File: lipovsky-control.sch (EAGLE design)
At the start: 43 parts, among them J5 AVRISP0.1", P1 M04-929P, P2 M04-929P, P3 M04-929P, P4 M04-929P, U1 ATTINYX4A8MU, U2 MIC2288YD5, U3 MIC2288YD5, U7 LTV-816S

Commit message: .
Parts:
- renumbered U7 to U4
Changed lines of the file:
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@@
 <parts>
 <part name="R1" library="dubec" deviceset="POT" device="5K" value="POT5K"/>
-<part name="U7" library="dubec" deviceset="LTV-8" device="16S"/>
+<part name="U4" library="dubec" deviceset="LTV-8" device="16S"/>
 <part name="R3" library="dubec" deviceset="RES" device="330_16" value="RES330_16"/>
 <part name="U1" library="dubec" deviceset="ATTINYX4A" device="8MU"/>
@@
 <instances>
 <instance part="R1" gate="G$1" x="55.88" y="-43.18" rot="R180"/>
-<instance part="U7" gate="G$1" x="66.04" y="-25.4" rot="MR0"/>
+<instance part="U4" gate="G$1" x="66.04" y="-25.4" rot="MR0"/>
 <instance part="R3" gate="G$1" x="55.88" y="-33.02" rot="R90"/>
 <instance part="U1" gate="G$1" x="12.7" y="22.86"/>
@@
 <net name="FB" class="0">
 <segment>
-<pinref part="U7" gate="G$1" pin="E"/>
+<pinref part="U4" gate="G$1" pin="E"/>
 <wire x1="58.42" y1="-27.94" x2="55.88" y2="-27.94" width="0.1524" layer="91"/>
 <label x="53.34" y="-27.94" size="1.778" layer="95" rot="R90" xref="yes"/>
@@
 <net name="OPTO_A" class="0">
 <segment>
-<pinref part="U7" gate="G$1" pin="A"/>
+<pinref part="U4" gate="G$1" pin="A"/>
 <wire x1="73.66" y1="-22.86" x2="76.2" y2="-22.86" width="0.1524" layer="91"/>
 <label x="76.2" y="-22.86" size="1.778" layer="95" xref="yes"/>
@@
 <net name="OPTO_C" class="0">
 <segment>
-<pinref part="U7" gate="G$1" pin="K"/>
+<pinref part="U4" gate="G$1" pin="K"/>
 <wire x1="73.66" y1="-27.94" x2="76.2" y2="-27.94" width="0.1524" layer="91"/>
 <label x="76.2" y="-27.94" size="1.778" layer="95" xref="yes"/>
@@
 </segment>
 <segment>
-<pinref part="U7" gate="G$1" pin="C"/>
+<pinref part="U4" gate="G$1" pin="C"/>
 <wire x1="58.42" y1="-22.86" x2="55.88" y2="-22.86" width="0.1524" layer="91"/>
 <wire x1="55.88" y1="-22.86" x2="55.88" y2="-17.78" width="0.1524" layer="91"/>

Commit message: tidy
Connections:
- removed net !OE: J5.SCK, P3.3, U1.PA4
- removed net CP: J5.MISO, P3.2, U1.PA5
- removed net DS: J5.MOSI, P3.1, U1.PA6
- new net !S_RESET: P3.1
- new net MISO: J5.MISO, U1.PA5
- new net SCL: J5.SCK, P3.2, U1.PA4
- new net SDA: J5.MOSI, P3.3, U1.PA6
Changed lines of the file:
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@@
 </segment>
 </net>
-<net name="!OE" class="0">
-<segment>
-<label x="78.74" y="35.56" size="1.27" layer="95" rot="R90" xref="yes"/>
-<wire x1="78.74" y1="33.02" x2="78.74" y2="35.56" width="0.1524" layer="91"/>
-<pinref part="P3" gate="G$1" pin="3"/>
-</segment>
-<segment>
-<label x="-10.16" y="17.78" size="1.27" layer="95" rot="R180" xref="yes"/>
-<pinref part="U1" gate="G$1" pin="PA4"/>
-<wire x1="-10.16" y1="17.78" x2="2.54" y2="17.78" width="0.1524" layer="91"/>
-</segment>
-<segment>
-<pinref part="J5" gate="G$1" pin="SCK"/>
-<wire x1="119.38" y1="22.86" x2="121.92" y2="20.32" width="0.1524" layer="91"/>
-<label x="121.92" y="20.32" size="1.27" layer="95" xref="yes"/>
-</segment>
-</net>
-<net name="CP" class="0">
-<segment>
-<label x="81.28" y="35.56" size="1.27" layer="95" rot="R90" xref="yes"/>
-<wire x1="81.28" y1="33.02" x2="81.28" y2="35.56" width="0.1524" layer="91"/>
-<pinref part="P3" gate="G$1" pin="2"/>
-</segment>
+<net name="MISO" class="0">
 <segment>
 <label x="-10.16" y="15.24" size="1.27" layer="95" rot="R180" xref="yes"/>
@@
 <wire x1="119.38" y1="17.78" x2="121.92" y2="15.24" width="0.1524" layer="91"/>
 <label x="121.92" y="15.24" size="1.27" layer="95" xref="yes"/>
-</segment>
-</net>
-<net name="DS" class="0">
-<segment>
-<label x="83.82" y="35.56" size="1.27" layer="95" rot="R90" xref="yes"/>
-<wire x1="83.82" y1="33.02" x2="83.82" y2="35.56" width="0.1524" layer="91"/>
-<pinref part="P3" gate="G$1" pin="1"/>
-</segment>
-<segment>
-<label x="33.02" y="27.94" size="1.27" layer="95" xref="yes"/>
-<pinref part="U1" gate="G$1" pin="PA6"/>
-<wire x1="33.02" y1="27.94" x2="22.86" y2="27.94" width="0.1524" layer="91"/>
-</segment>
-<segment>
-<pinref part="J5" gate="G$1" pin="MOSI"/>
-<wire x1="104.14" y1="22.86" x2="101.6" y2="20.32" width="0.1524" layer="91"/>
-<label x="101.6" y="20.32" size="1.27" layer="95" rot="R180" xref="yes"/>
 </segment>
 </net>
@@
 </segment>
 </net>
+<net name="SDA" class="0">
+<segment>
+<pinref part="P3" gate="G$1" pin="3"/>
+<wire x1="78.74" y1="33.02" x2="78.74" y2="35.56" width="0.1524" layer="91"/>
+<label x="78.74" y="35.56" size="1.27" layer="95" rot="R90" xref="yes"/>
+</segment>
+<segment>
+<label x="33.02" y="27.94" size="1.27" layer="95" xref="yes"/>
+<pinref part="U1" gate="G$1" pin="PA6"/>
+<wire x1="33.02" y1="27.94" x2="22.86" y2="27.94" width="0.1524" layer="91"/>
+</segment>
+<segment>
+<pinref part="J5" gate="G$1" pin="MOSI"/>
+<wire x1="104.14" y1="22.86" x2="101.6" y2="20.32" width="0.1524" layer="91"/>
+<label x="101.6" y="20.32" size="1.27" layer="95" rot="R180" xref="yes"/>
+</segment>
+</net>
+<net name="SCL" class="0">
+<segment>
+<pinref part="P3" gate="G$1" pin="2"/>
+<wire x1="81.28" y1="33.02" x2="81.28" y2="35.56" width="0.1524" layer="91"/>
+<label x="81.28" y="35.56" size="1.27" layer="95" rot="R90" xref="yes"/>
+</segment>
+<segment>
+<label x="-10.16" y="17.78" size="1.27" layer="95" rot="R180" xref="yes"/>
+<pinref part="U1" gate="G$1" pin="PA4"/>
+<wire x1="-10.16" y1="17.78" x2="2.54" y2="17.78" width="0.1524" layer="91"/>
+</segment>
+<segment>
+<pinref part="J5" gate="G$1" pin="SCK"/>
+<wire x1="119.38" y1="22.86" x2="121.92" y2="20.32" width="0.1524" layer="91"/>
+<label x="121.92" y="20.32" size="1.27" layer="95" xref="yes"/>
+</segment>
+</net>
+<net name="!S_RESET" class="0">
+<segment>
+<pinref part="P3" gate="G$1" pin="1"/>
+<wire x1="83.82" y1="33.02" x2="83.82" y2="35.56" width="0.1524" layer="91"/>
+<label x="83.82" y="35.56" size="1.27" layer="95" rot="R90" xref="yes"/>
+</segment>
+</net>

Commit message: neverending gilding
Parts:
- added R16, R17: RES4.7K_16, dubec:RES4.7K_16
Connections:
- net !RESET: now also R15.1; no longer R15.2
- net +5V: now also R15.2, R16.2, R17.1; no longer R15.1
- net SCL: now also R17.2
- net SDA: now also R16.1
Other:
- moved on the sheet: R10, R15, R7, R8, R9
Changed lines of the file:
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@@
 <part name="J5" library="dubec" deviceset="AVRISP" device="0.1&quot;" value="AVRISP0.1&quot;"/>
 <part name="R15" library="dubec" deviceset="RES" device="10K_16"/>
+<part name="R16" library="dubec" deviceset="RES" device="4.7K_16" value="RES4.7K_16"/>
+<part name="R17" library="dubec" deviceset="RES" device="4.7K_16" value="RES4.7K_16"/>
 </parts>
 <sheets>
@@
 <instance part="D4" gate="G$1" x="-2.54" y="-22.86"/>
 <instance part="D5" gate="G$1" x="-2.54" y="-38.1"/>
-<instance part="R7" gate="G$1" x="27.94" y="25.4"/>
-<instance part="R8" gate="G$1" x="27.94" y="17.78"/>
-<instance part="R9" gate="G$1" x="27.94" y="20.32"/>
-<instance part="R10" gate="G$1" x="27.94" y="22.86"/>
+<instance part="R7" gate="G$1" x="30.48" y="25.4"/>
+<instance part="R8" gate="G$1" x="30.48" y="17.78"/>
+<instance part="R9" gate="G$1" x="30.48" y="20.32"/>
+<instance part="R10" gate="G$1" x="30.48" y="22.86"/>
 <instance part="R11" gate="G$1" x="5.08" y="-40.64" rot="R90"/>
 <instance part="R12" gate="G$1" x="10.16" y="-35.56" rot="R180"/>
@@
 <instance part="C3" gate="G$1" x="43.18" y="-35.56" rot="R90"/>
 <instance part="J5" gate="G$1" x="111.76" y="22.86"/>
-<instance part="R15" gate="G$1" x="25.4" y="10.16" rot="R90"/>
+<instance part="R15" gate="G$1" x="30.48" y="15.24"/>
+<instance part="R16" gate="G$1" x="30.48" y="27.94"/>
+<instance part="R17" gate="G$1" x="-5.08" y="17.78"/>
 </instances>
 <busses>
@@
 <segment>
 <pinref part="U1" gate="G$1" pin="PB3"/>
-<wire x1="22.86" y1="15.24" x2="25.4" y2="15.24" width="0.1524" layer="91"/>
-<label x="33.02" y="15.24" size="1.27" layer="95" xref="yes"/>
-<pinref part="R15" gate="G$1" pin="2"/>
-<wire x1="25.4" y1="15.24" x2="33.02" y2="15.24" width="0.1524" layer="91"/>
-<wire x1="25.4" y1="15.24" x2="25.4" y2="12.7" width="0.1524" layer="91"/>
-<junction x="25.4" y="15.24"/>
+<label x="25.4" y="15.24" size="1.27" layer="95" rot="R270" xref="yes"/>
+<pinref part="R15" gate="G$1" pin="1"/>
+<wire x1="22.86" y1="15.24" x2="27.94" y2="15.24" width="0.1524" layer="91"/>
 </segment>
 <segment>
@@
 </segment>
 <segment>
-<pinref part="R15" gate="G$1" pin="1"/>
-<wire x1="25.4" y1="7.62" x2="25.4" y2="5.08" width="0.1524" layer="91"/>
-<label x="25.4" y="5.08" size="1.27" layer="95" rot="R270" xref="yes"/>
-</segment>
-<segment>
 <pinref part="J5" gate="G$1" pin="VCC"/>
 <wire x1="104.14" y1="17.78" x2="101.6" y2="15.24" width="0.1524" layer="91"/>
 <label x="101.6" y="15.24" size="1.27" layer="95" rot="R180" xref="yes"/>
+</segment>
+<segment>
+<pinref part="R17" gate="G$1" pin="1"/>
+<wire x1="-7.62" y1="17.78" x2="-10.16" y2="17.78" width="0.1524" layer="91"/>
+<label x="-10.16" y="17.78" size="1.27" layer="95" rot="R180" xref="yes"/>
+</segment>
+<segment>
+<pinref part="R16" gate="G$1" pin="2"/>
+<wire x1="33.02" y1="27.94" x2="35.56" y2="27.94" width="0.1524" layer="91"/>
+<label x="35.56" y="27.94" size="1.27" layer="95" xref="yes"/>
+</segment>
+<segment>
+<pinref part="R15" gate="G$1" pin="2"/>
+<wire x1="33.02" y1="15.24" x2="35.56" y2="15.24" width="0.1524" layer="91"/>
+<label x="35.56" y="15.24" size="1.27" layer="95" xref="yes"/>
 </segment>
 </net>
@@
 </segment>
 <segment>
-<label x="33.02" y="25.4" size="1.27" layer="95" xref="yes"/>
+<label x="35.56" y="25.4" size="1.27" layer="95" xref="yes"/>
 <pinref part="R7" gate="G$1" pin="2"/>
-<wire x1="30.48" y1="25.4" x2="33.02" y2="25.4" width="0.1524" layer="91"/>
+<wire x1="33.02" y1="25.4" x2="35.56" y2="25.4" width="0.1524" layer="91"/>
 </segment>
 </net>
@@
 </segment>
 <segment>
-<label x="33.02" y="17.78" size="1.27" layer="95" xref="yes"/>
+<label x="35.56" y="17.78" size="1.27" layer="95" xref="yes"/>
 <pinref part="R8" gate="G$1" pin="2"/>
-<wire x1="30.48" y1="17.78" x2="33.02" y2="17.78" width="0.1524" layer="91"/>
+<wire x1="33.02" y1="17.78" x2="35.56" y2="17.78" width="0.1524" layer="91"/>
 </segment>
 </net>
@@
 </segment>
 <segment>
-<label x="33.02" y="20.32" size="1.27" layer="95" xref="yes"/>
+<label x="35.56" y="20.32" size="1.27" layer="95" xref="yes"/>
 <pinref part="R9" gate="G$1" pin="2"/>
-<wire x1="33.02" y1="20.32" x2="30.48" y2="20.32" width="0.1524" layer="91"/>
+<wire x1="35.56" y1="20.32" x2="33.02" y2="20.32" width="0.1524" layer="91"/>
 </segment>
 </net>
@@
 </segment>
 <segment>
-<label x="33.02" y="22.86" size="1.27" layer="95" xref="yes"/>
+<label x="35.56" y="22.86" size="1.27" layer="95" xref="yes"/>
 <pinref part="R10" gate="G$1" pin="2"/>
-<wire x1="33.02" y1="22.86" x2="30.48" y2="22.86" width="0.1524" layer="91"/>
+<wire x1="35.56" y1="22.86" x2="33.02" y2="22.86" width="0.1524" layer="91"/>
 </segment>
 </net>
@@
 <pinref part="U1" gate="G$1" pin="PB0"/>
 <pinref part="R10" gate="G$1" pin="1"/>
-<wire x1="22.86" y1="22.86" x2="25.4" y2="22.86" width="0.1524" layer="91"/>
+<wire x1="22.86" y1="22.86" x2="27.94" y2="22.86" width="0.1524" layer="91"/>
 </segment>
 </net>
@@
 <pinref part="U1" gate="G$1" pin="PB1"/>
 <pinref part="R9" gate="G$1" pin="1"/>
-<wire x1="22.86" y1="20.32" x2="25.4" y2="20.32" width="0.1524" layer="91"/>
+<wire x1="22.86" y1="20.32" x2="27.94" y2="20.32" width="0.1524" layer="91"/>
 </segment>
 </net>
@@
 <pinref part="U1" gate="G$1" pin="PB2"/>
 <pinref part="R8" gate="G$1" pin="1"/>
-<wire x1="22.86" y1="17.78" x2="25.4" y2="17.78" width="0.1524" layer="91"/>
+<wire x1="22.86" y1="17.78" x2="27.94" y2="17.78" width="0.1524" layer="91"/>
 </segment>
 </net>
@@
 <pinref part="U1" gate="G$1" pin="PA7"/>
 <pinref part="R7" gate="G$1" pin="1"/>
-<wire x1="22.86" y1="25.4" x2="25.4" y2="25.4" width="0.1524" layer="91"/>
+<wire x1="22.86" y1="25.4" x2="27.94" y2="25.4" width="0.1524" layer="91"/>
 </segment>
 </net>
@@
 </segment>
 <segment>
-<label x="33.02" y="27.94" size="1.27" layer="95" xref="yes"/>
+<label x="25.4" y="27.94" size="1.27" layer="95" rot="R90" xref="yes"/>
 <pinref part="U1" gate="G$1" pin="PA6"/>
-<wire x1="33.02" y1="27.94" x2="22.86" y2="27.94" width="0.1524" layer="91"/>
+<pinref part="R16" gate="G$1" pin="1"/>
+<wire x1="22.86" y1="27.94" x2="27.94" y2="27.94" width="0.1524" layer="91"/>
 </segment>
 <segment>
@@
 </segment>
 <segment>
-<label x="-10.16" y="17.78" size="1.27" layer="95" rot="R180" xref="yes"/>
+<label x="0" y="17.78" size="1.27" layer="95" rot="R90" xref="yes"/>
 <pinref part="U1" gate="G$1" pin="PA4"/>
-<wire x1="-10.16" y1="17.78" x2="2.54" y2="17.78" width="0.1524" layer="91"/>
-</segment>
-<segment>
+<pinref part="R17" gate="G$1" pin="2"/>
+<wire x1="2.54" y1="17.78" x2="-2.54" y2="17.78" width="0.1524" layer="91"/>
+</segment>
+<segment>

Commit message: tweaks
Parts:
- added U$2: JUMPER-PAD, dubec:JUMPER-PAD
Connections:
- net !S_RESET: now also U$2.1
- net MISO: now also U$2.2
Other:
- moved on the sheet: C1, C2, J5, P1, P2, P3, P4, R10, R13, R15, R16, R17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

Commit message: Connector pin reordering
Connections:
- net +5V: now also P4.4; no longer P4.2
- net +8V: now also P4.2; no longer P4.1
- net OPTO_C: now also P2.4; no longer P2.2
- net S+: now also P4.1; no longer P4.3
- net S-: now also P2.2, P3.3, P4.3; no longer P2.4, P3.4, P4.4
- net SCL: now also P3.4; no longer P3.2
- net SDA: now also P3.2; no longer P3.3
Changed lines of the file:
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@@
 </segment>
 <segment>
-<label x="93.98" y="12.7" size="1.27" layer="95" rot="R270" xref="yes"/>
-<wire x1="93.98" y1="15.24" x2="93.98" y2="12.7" width="0.1524" layer="91"/>
-<pinref part="P2" gate="G$1" pin="4"/>
-</segment>
-<segment>
-<label x="86.36" y="35.56" size="1.27" layer="95" rot="R90" xref="yes"/>
-<wire x1="86.36" y1="33.02" x2="86.36" y2="35.56" width="0.1524" layer="91"/>
-<pinref part="P3" gate="G$1" pin="4"/>
-</segment>
-<segment>
-<label x="66.04" y="35.56" size="1.27" layer="95" rot="R90" xref="yes"/>
-<wire x1="66.04" y1="33.02" x2="66.04" y2="35.56" width="0.1524" layer="91"/>
-<pinref part="P4" gate="G$1" pin="4"/>
+<label x="88.9" y="12.7" size="1.27" layer="95" rot="R270" xref="yes"/>
+<pinref part="P2" gate="G$1" pin="2"/>
+<wire x1="88.9" y1="12.7" x2="88.9" y2="15.24" width="0.1524" layer="91"/>
+</segment>
+<segment>
+<label x="88.9" y="35.56" size="1.27" layer="95" rot="R90" xref="yes"/>
+<pinref part="P3" gate="G$1" pin="3"/>
+<wire x1="88.9" y1="35.56" x2="88.9" y2="33.02" width="0.1524" layer="91"/>
+</segment>
+<segment>
+<label x="68.58" y="35.56" size="1.27" layer="95" rot="R90" xref="yes"/>
+<pinref part="P4" gate="G$1" pin="3"/>
+<wire x1="68.58" y1="35.56" x2="68.58" y2="33.02" width="0.1524" layer="91"/>
 </segment>
 <segment>
@@
 <segment>
 <label x="91.44" y="12.7" size="1.27" layer="95" rot="R270" xref="yes"/>
-<wire x1="91.44" y1="15.24" x2="91.44" y2="12.7" width="0.1524" layer="91"/>
 <pinref part="P2" gate="G$1" pin="3"/>
+<wire x1="91.44" y1="12.7" x2="91.44" y2="15.24" width="0.1524" layer="91"/>
 </segment>
 </net>
@@
 </segment>
 <segment>
-<label x="88.9" y="12.7" size="1.27" layer="95" rot="R270" xref="yes"/>
-<wire x1="88.9" y1="15.24" x2="88.9" y2="12.7" width="0.1524" layer="91"/>
-<pinref part="P2" gate="G$1" pin="2"/>
+<label x="93.98" y="12.7" size="1.27" layer="95" rot="R270" xref="yes"/>
+<pinref part="P2" gate="G$1" pin="4"/>
+<wire x1="93.98" y1="12.7" x2="93.98" y2="15.24" width="0.1524" layer="91"/>
 </segment>
 </net>
@@
 </segment>
 <segment>
-<label x="71.12" y="35.56" size="1.27" layer="95" rot="R90" xref="yes"/>
-<pinref part="P4" gate="G$1" pin="2"/>
-<wire x1="71.12" y1="35.56" x2="71.12" y2="33.02" width="0.1524" layer="91"/>
+<label x="66.04" y="35.56" size="1.27" layer="95" rot="R90" xref="yes"/>
+<pinref part="P4" gate="G$1" pin="4"/>
+<wire x1="66.04" y1="35.56" x2="66.04" y2="33.02" width="0.1524" layer="91"/>
 </segment>
 <segment>
@@
 <net name="S+" class="0">
 <segment>
-<label x="68.58" y="35.56" size="1.27" layer="95" rot="R90" xref="yes"/>
-<pinref part="P4" gate="G$1" pin="3"/>
-<wire x1="68.58" y1="35.56" x2="68.58" y2="33.02" width="0.1524" layer="91"/>
+<label x="73.66" y="35.56" size="1.27" layer="95" rot="R90" xref="yes"/>
+<pinref part="P4" gate="G$1" pin="1"/>
+<wire x1="73.66" y1="35.56" x2="73.66" y2="33.02" width="0.1524" layer="91"/>
 </segment>
 <segment>
@@
 <net name="+8V" class="0">
 <segment>
-<label x="73.66" y="35.56" size="1.27" layer="95" rot="R90" xref="yes"/>
-<wire x1="73.66" y1="33.02" x2="73.66" y2="35.56" width="0.1524" layer="91"/>
-<pinref part="P4" gate="G$1" pin="1"/>
+<label x="71.12" y="35.56" size="1.27" layer="95" rot="R90" xref="yes"/>
+<pinref part="P4" gate="G$1" pin="2"/>
+<wire x1="71.12" y1="35.56" x2="71.12" y2="33.02" width="0.1524" layer="91"/>
 </segment>
 <segment>
@@
 <net name="SDA" class="0">
 <segment>
-<pinref part="P3" gate="G$1" pin="3"/>
-<wire x1="88.9" y1="33.02" x2="88.9" y2="35.56" width="0.1524" layer="91"/>
-<label x="88.9" y="35.56" size="1.27" layer="95" rot="R90" xref="yes"/>
+<label x="91.44" y="35.56" size="1.27" layer="95" rot="R90" xref="yes"/>
+<pinref part="P3" gate="G$1" pin="2"/>
+<wire x1="91.44" y1="35.56" x2="91.44" y2="33.02" width="0.1524" layer="91"/>
 </segment>
 <segment>
@@
 <net name="SCL" class="0">
 <segment>
-<pinref part="P3" gate="G$1" pin="2"/>
-<wire x1="91.44" y1="33.02" x2="91.44" y2="35.56" width="0.1524" layer="91"/>
-<label x="91.44" y="35.56" size="1.27" layer="95" rot="R90" xref="yes"/>
-</segment>
-<segment>
+<label x="86.36" y="35.56" size="1.27" layer="95" rot="R90" xref="yes"/>
+<pinref part="P3" gate="G$1" pin="4"/>
+<wire x1="86.36" y1="35.56" x2="86.36" y2="33.02" width="0.1524" layer="91"/>
+</segment>
+<segment>

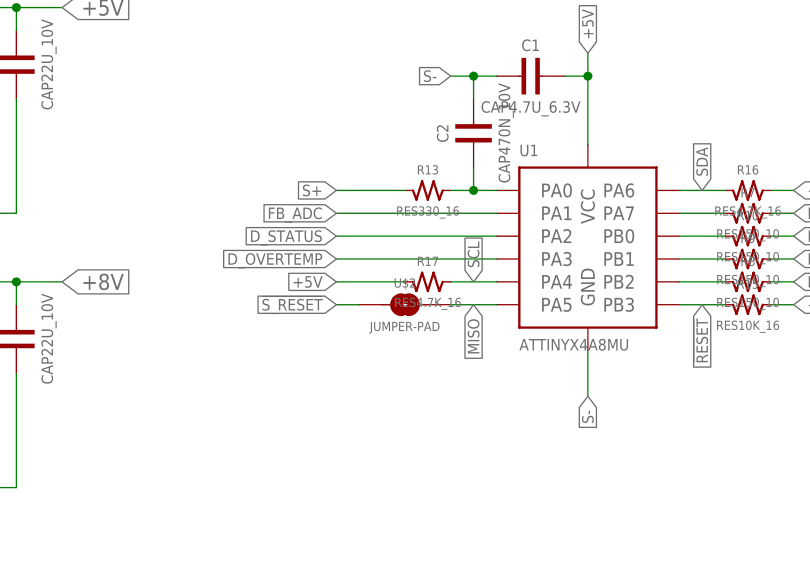
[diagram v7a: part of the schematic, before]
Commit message: Label fix
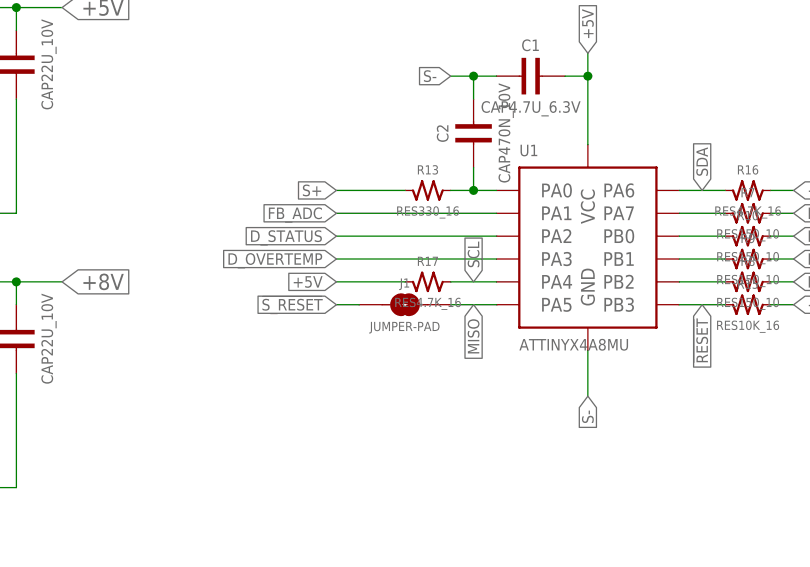
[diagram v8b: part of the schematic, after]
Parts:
- renumbered U$2 to J1
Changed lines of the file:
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@@
 <part name="R16" library="dubec" deviceset="RES" device="4.7K_16" value="RES4.7K_16"/>
 <part name="R17" library="dubec" deviceset="RES" device="4.7K_16" value="RES4.7K_16"/>
-<part name="U$2" library="dubec" deviceset="JUMPER-PAD" device=""/>
+<part name="J1" library="dubec" deviceset="JUMPER-PAD" device=""/>
 </parts>
 <sheets>
@@
 <instance part="R16" gate="G$1" x="40.64" y="27.94"/>
 <instance part="R17" gate="G$1" x="5.08" y="17.78"/>
-<instance part="U$2" gate="G$1" x="2.54" y="15.24"/>
+<instance part="J1" gate="G$1" x="2.54" y="15.24"/>
 </instances>
 <busses>
@@
 <label x="10.16" y="15.24" size="1.27" layer="95" rot="R270" xref="yes"/>
 <pinref part="U1" gate="G$1" pin="PA5"/>
-<pinref part="U$2" gate="G$1" pin="2"/>
+<pinref part="J1" gate="G$1" pin="2"/>
 <wire x1="12.7" y1="15.24" x2="7.62" y2="15.24" width="0.1524" layer="91"/>
 </segment>
@@
 </segment>
 <segment>
-<pinref part="U$2" gate="G$1" pin="1"/>
+<pinref part="J1" gate="G$1" pin="1"/>
 <wire x1="-2.54" y1="15.24" x2="-5.08" y2="15.24" width="0.1524" layer="91"/>
 <label x="-5.08" y="15.24" size="1.27" layer="95" rot="R180" xref="yes"/>
